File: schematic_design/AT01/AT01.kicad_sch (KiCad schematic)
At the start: 11 parts

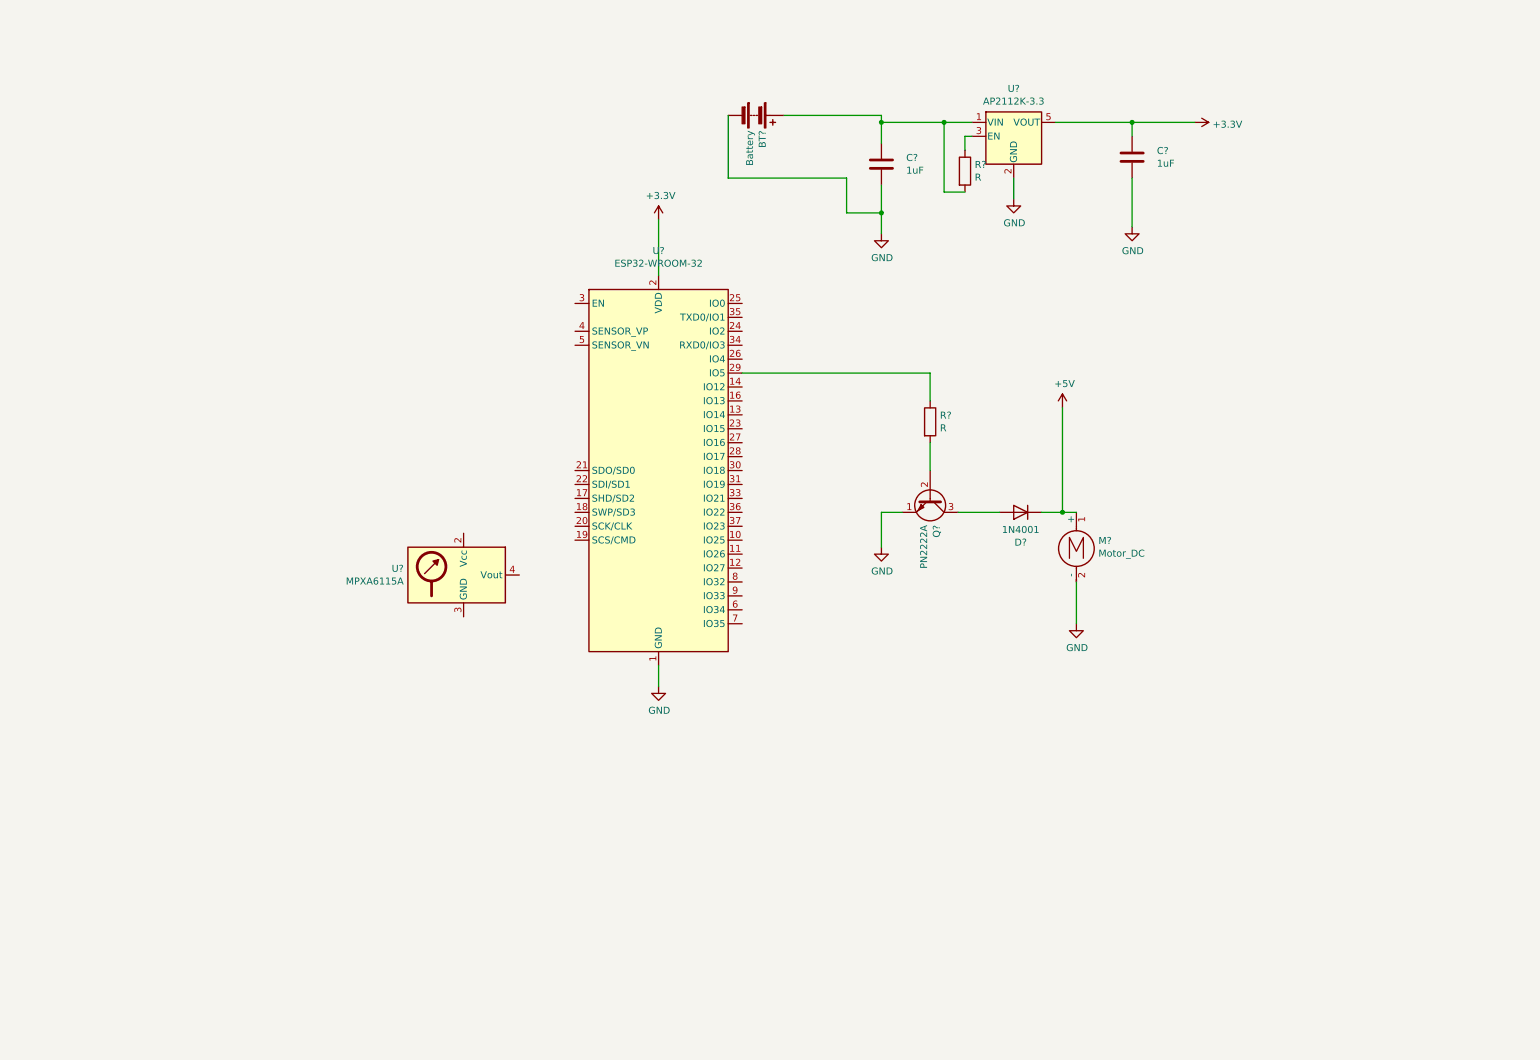
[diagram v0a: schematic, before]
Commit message: added pressure sensor circuit
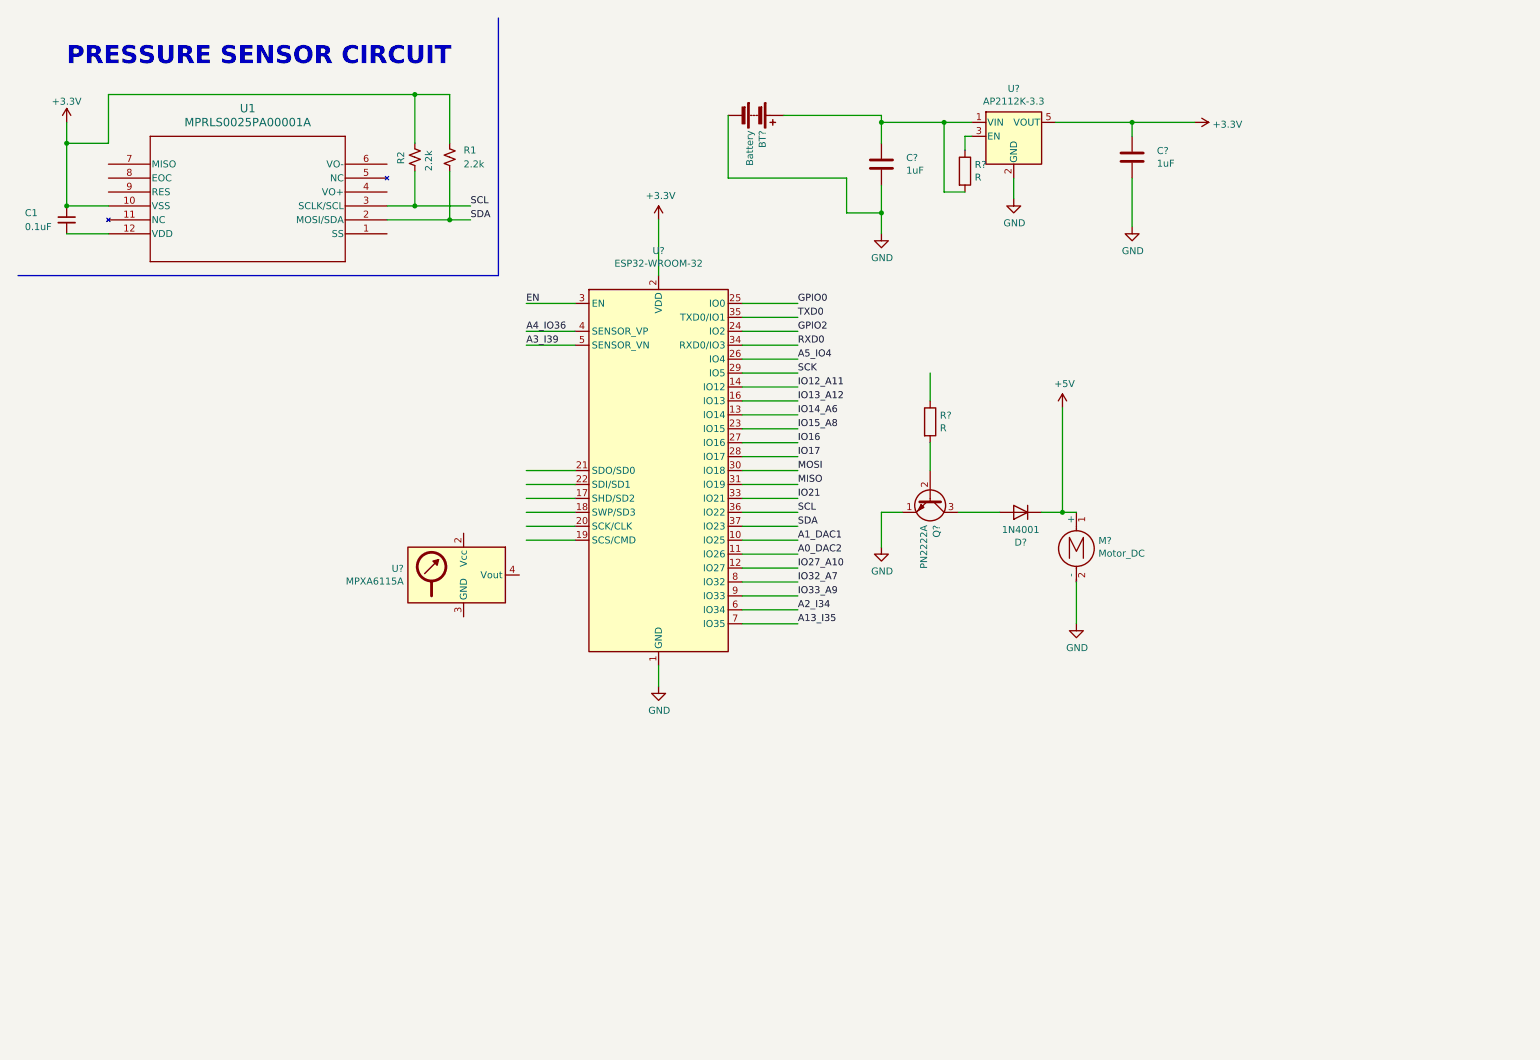
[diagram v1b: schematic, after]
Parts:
- added C1: 0.1uF, symbol Device:C_Small
- added R1, R2: 2.2k, symbol Device:R_Small_US
- added U1: MPRLS0025PA00001A, MPRLS_HNW, symbol MPRLS0025PA00001A:MPRLS0025PA00001A
- U?: footprint RF_Module:ESP32-WROOM-32 -> RF_Module:ESP32-WROOM-32D; symbol RF_Module:ESP32-WROOM-32 -> RF_Module:ESP32-WROOM-32D
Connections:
- net +3.3V: now also C1.1, R1.1, R2.1, U1.10 (VSS)
- net A1_DAC1: now reaches U?.10 (IO25)
- net A0_DAC2: now reaches U?.11 (IO26)
- net IO27_A10: now reaches U?.12 (IO27)
- net IO14_A6: now reaches U?.13 (IO14)
- net IO12_A11: now reaches U?.14 (IO12)
- net IO13_A12: now reaches U?.16 (IO13)
- net IO15_A8: now reaches U?.23 (IO15)
- net GPIO2: now reaches U?.24 (IO2)
- net GPIO0: now reaches U?.25 (IO0)
- net A5_IO4: now reaches U?.26 (IO4)
- net IO16: now reaches U?.27 (IO16)
- net IO17: now reaches U?.28 (IO17)
- net at R?.1: no longer U?.29 (IO5)
- net EN: now reaches U?.3 (EN)
- net MOSI: now reaches U?.30 (IO18)
- net MISO: now reaches U?.31 (IO19)
- net IO21: now reaches U?.33 (IO21)
- net RXD0: now reaches U?.34 (RXD0/IO3)
- net TXD0: now reaches U?.35 (TXD0/IO1)
- net SCL: now reaches U?.36 (IO22)
- net SCL: now also R2.2, U1.3 (SCLK/SCL)
- net SDA: now reaches U?.37 (IO23)
- net SDA: now also R1.2, U1.2 (MOSI/SDA)
- net A4_IO36: now reaches U?.4 (SENSOR_VP)
- net A3_I39: now reaches U?.5 (SENSOR_VN)
- net A2_I34: now reaches U?.6 (IO34)
- net A13_I35: now reaches U?.7 (IO35)
- net IO32_A7: now reaches U?.8 (IO32)
- net IO33_A9: now reaches U?.9 (IO33)
- new net: C1.2, U1.12 (VDD)
- new net SCK: U?.29 (IO5)
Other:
- note added: "PRESSURE SENSOR CIRCUIT"

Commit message: adding power supply circuit to schematic
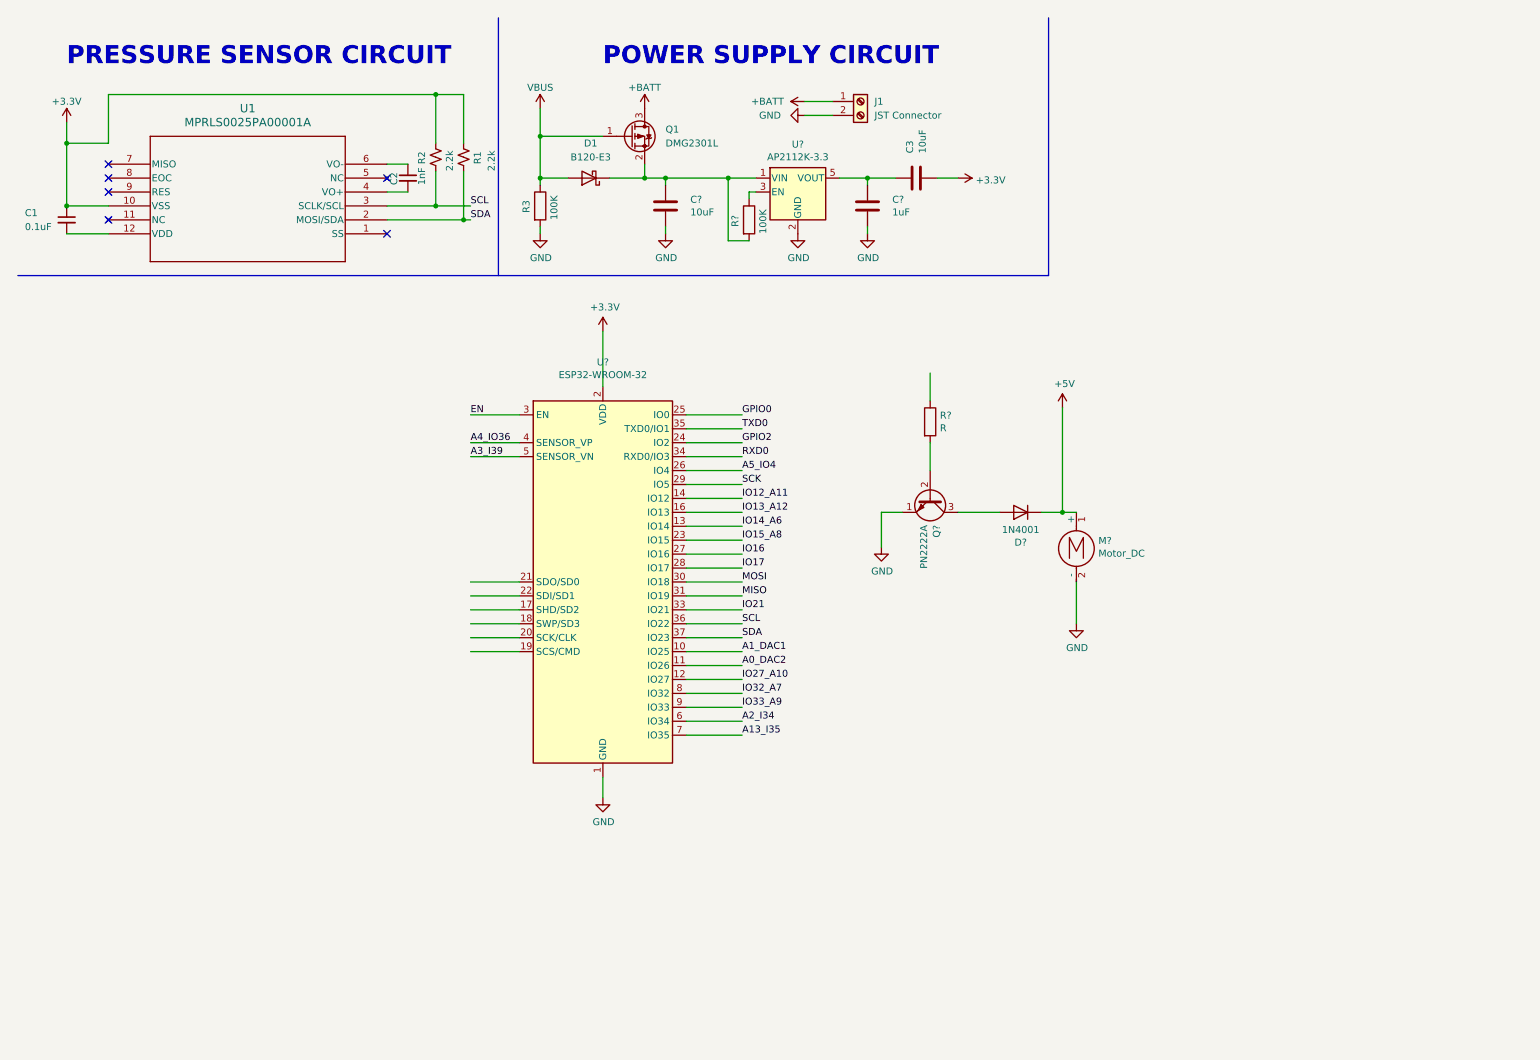
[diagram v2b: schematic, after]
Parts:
- removed BT?: Battery, symbol Device:Battery
- removed U?: MPXA6115A, symbol Sensor_Pressure:MPXA6115A
- added C2: 1nF, symbol Device:C_Small
- added C3: 10uF, symbol Device:C
- added D1: B120-E3, Diode_SMD:D_SMA, symbol Diode:B120-E3
- added J1: JST Connector, symbol Connector:Screw_Terminal_01x02
- added Q1: DMG2301L, Package_TO_SOT_SMD:SOT-23, symbol Transistor_FET:DMG2301L
- added R3: 100K, symbol Device:R
- C?: value 1uF -> 10uF
- R?: value R -> 100K
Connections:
- net +3.3V: now also C3.2; no longer C?.1, U?.5 (VOUT)
- net GND: now also J1.2 (Pin_2), R3.2
- net at C?.1, R?.2, U?.1 (VIN): now also D1.1 (K), Q1.2 (S)
- net at U1.4 (VO+): now also C2.2
- net at U1.6 (VO-): now also C2.1
- new net: C3.1, C?.1, U?.5 (VOUT)
- new net +BATT: J1.1 (Pin_1), Q1.3 (D)
- new net VBUS: D1.2 (A), Q1.1 (G), R3.1
- no-connect marks 0 -> 6
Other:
- note added: "POWER SUPPLY CIRCUIT"
- moved on the sheet: C?, R1, R2, R?, U?

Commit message: adding motor drive schematic
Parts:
- removed C3: 10uF, symbol Device:C
- added M1: Motor_DC, symbol Motor:Motor_DC
- added U2: DRV8837, Package_SON:WSON-8-1EP_2x2mm_P0.5mm_EP0.9x1.6mm, symbol Driver_Motor:DRV8837
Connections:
- net +3.3V: now also C?.1, U?.5 (VOUT), U2.8 (VCC)
- net +BATT: now also U2.1 (VM)
- net GND: now also U2.4 (GND), U2.9 (GND)
- net IO12_A11: now also U2.7 (~{SLEEP})
- net IO16: now also U2.6 (IN1)
- new net: M1.1 (+), U2.2 (OUT1)
- new net: M1.2 (-), U2.3 (OUT2)
- new net IO15: U2.5 (IN2)
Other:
- note added: "MOTOR DRIVER CIRCUIT"

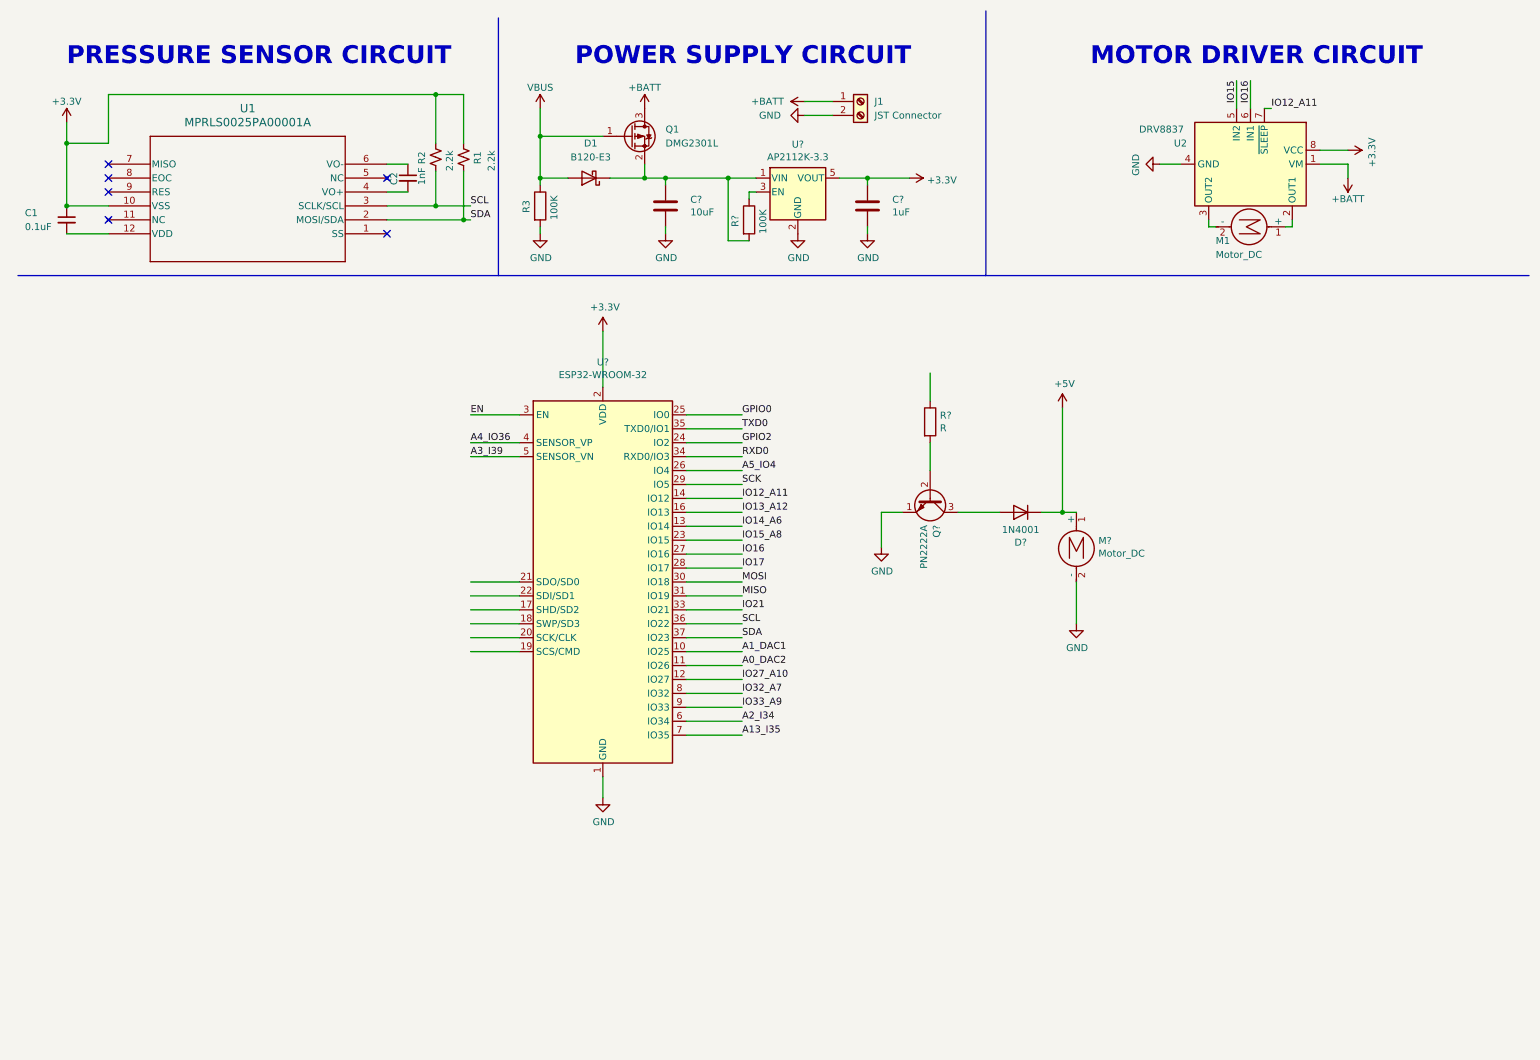
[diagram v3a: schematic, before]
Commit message: fixing motor driver schematic and adding reset schematic
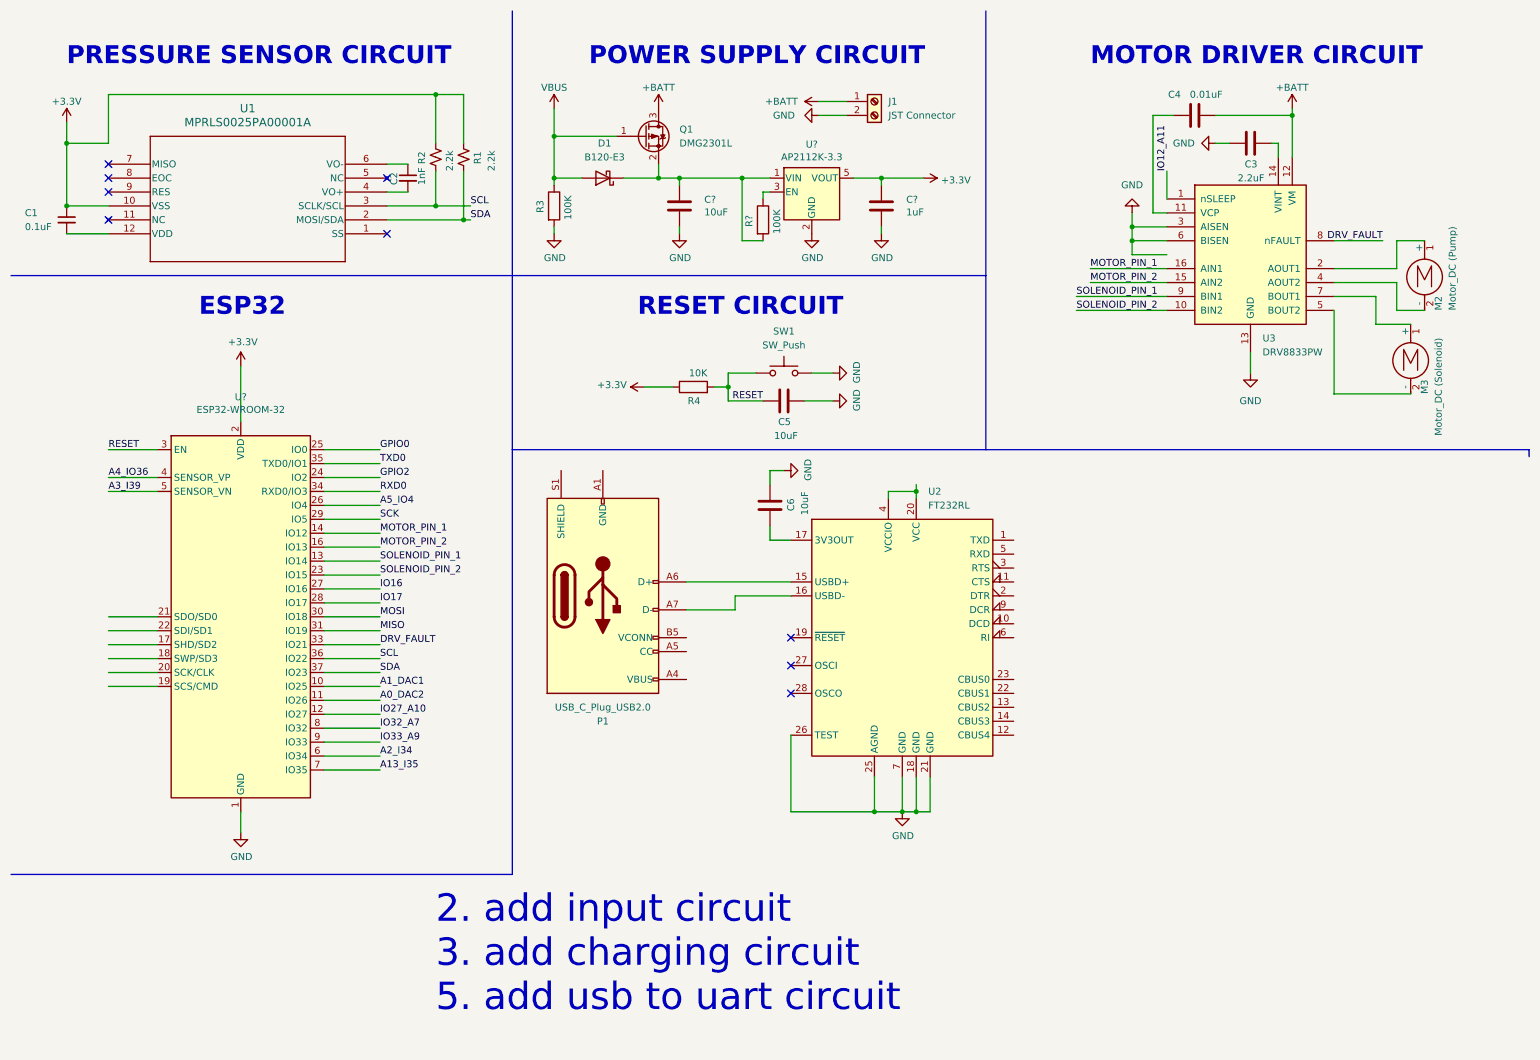
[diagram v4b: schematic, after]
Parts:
- removed D?: 1N4001, Diode_THT:D_DO-41_SOD81_P10.16mm_Horizontal, symbol Diode:1N4001
- removed M1, M?: Motor_DC, symbol Motor:Motor_DC
- removed Q?: PN2222A, Package_TO_SOT_THT:TO-92_Inline, symbol Transistor_BJT:PN2222A
- removed R?: R, symbol Device:R
- removed U2: DRV8837, Package_SON:WSON-8-1EP_2x2mm_P0.5mm_EP0.9x1.6mm, symbol Driver_Motor:DRV8837
- added C3: 2.2uF, symbol Device:C
- added C4: 0.01uF, symbol Device:C
- added C5, C6: 10uF, symbol Device:C
- added M2: Motor_DC (Pump), symbol Motor:Motor_DC
- added M3: Motor_DC (Solenoid), symbol Motor:Motor_DC
- added P1: USB_C_Plug_USB2.0, symbol Connector:USB_C_Plug_USB2.0
- added R4: 10K, symbol Device:R
- added SW1: SW_Push, symbol Switch:SW_Push
- added U2: FT232RL, Package_SO:SSOP-28_5.3x10.2mm_P0.65mm, symbol Interface_USB:FT232RL
- added U3: DRV8833PW, Package_SO:TSSOP-16_4.4x5mm_P0.65mm, symbol Driver_Motor:DRV8833PW
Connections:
- net +3.3V: now also R4.1
- net +BATT: now also C4.2, U3.12 (VM)
- net GND: now also C3.1, C5.2, C6.2, SW1.2, U2.18 (GND), U2.21 (GND), U2.25 (AGND), U2.26 (TEST), U2.7 (GND), U3.13 (GND), U3.3 (AISEN), U3.6 (BISEN)
- net IO12_A11: now also U3.1 (nSLEEP); no longer U?.14 (IO12)
- net EN renamed RESET
- net RESET: now also C5.1, R4.2, SW1.1
- net IO13_A12 renamed MOTOR_PIN_2
- net MOTOR_PIN_2: now also U3.15 (AIN2)
- net IO14_A6 renamed SOLENOID_PIN_1
- net SOLENOID_PIN_1: now also U3.9 (BIN1)
- net IO15_A8 renamed SOLENOID_PIN_2
- net SOLENOID_PIN_2: now also U3.10 (BIN2)
- net IO21 renamed DRV_FAULT
- net DRV_FAULT: now also U3.8 (nFAULT)
- new net: P1.A6 (D+), U2.15 (USBD+)
- new net: P1.A7 (D-), U2.16 (USBD-)
- new net: C6.1, U2.17 (3V3OUT)
- new net: U2.20 (VCC), U2.4 (VCCIO)
- new net: C4.1, U3.11 (VCP)
- new net: C3.2, U3.14 (VINT)
- new net: M2.1 (+), U3.2 (AOUT1)
- new net: M2.2 (-), U3.4 (AOUT2)
- new net: M3.2 (-), U3.5 (BOUT2)
- new net: M3.1 (+), U3.7 (BOUT1)
- new net: P1.A1 (GND), P1.A12 (GND), P1.B1 (GND), P1.B12 (GND)
- new net: P1.A4 (VBUS), P1.A9 (VBUS), P1.B4 (VBUS), P1.B9 (VBUS)
- new net MOTOR_PIN_1: U3.16 (AIN1), U?.14 (IO12)
- no-connect marks 6 -> 9
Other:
- note added: "2. add input circuit 3. add charging circuit 5. add usb to uart circuit"
- note added: "ESP32"
- note added: "RESET CIRCUIT"
- moved on the sheet: C?, D1, J1, Q1, R3, R?, U?
